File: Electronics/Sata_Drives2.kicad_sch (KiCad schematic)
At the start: 66 parts, among them J20 0877131001, J21 0877131001, Q10 NPN, Q11 PMOS, Q12 NPN, Q13 PMOS, Q14 PMOS, Q15 NPN, Q16 PMOS, Q17 NPN, U11 W25X40CLSN, U12 JMS561, Y2 30MHz

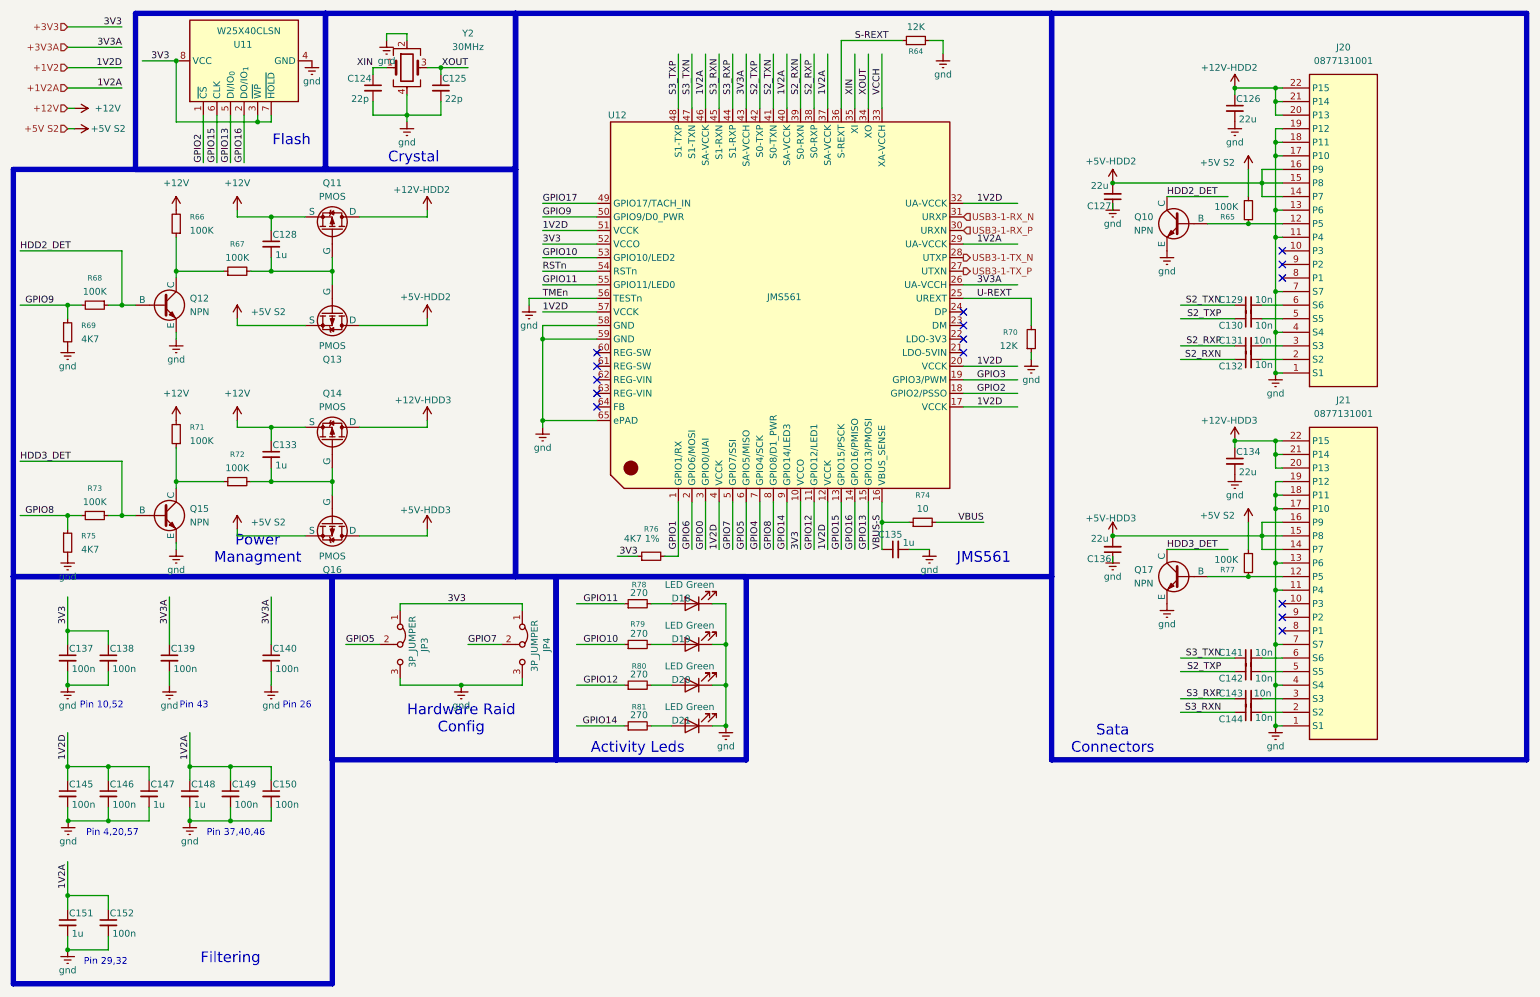
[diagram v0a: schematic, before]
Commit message: More pcb arangment, verticle ports
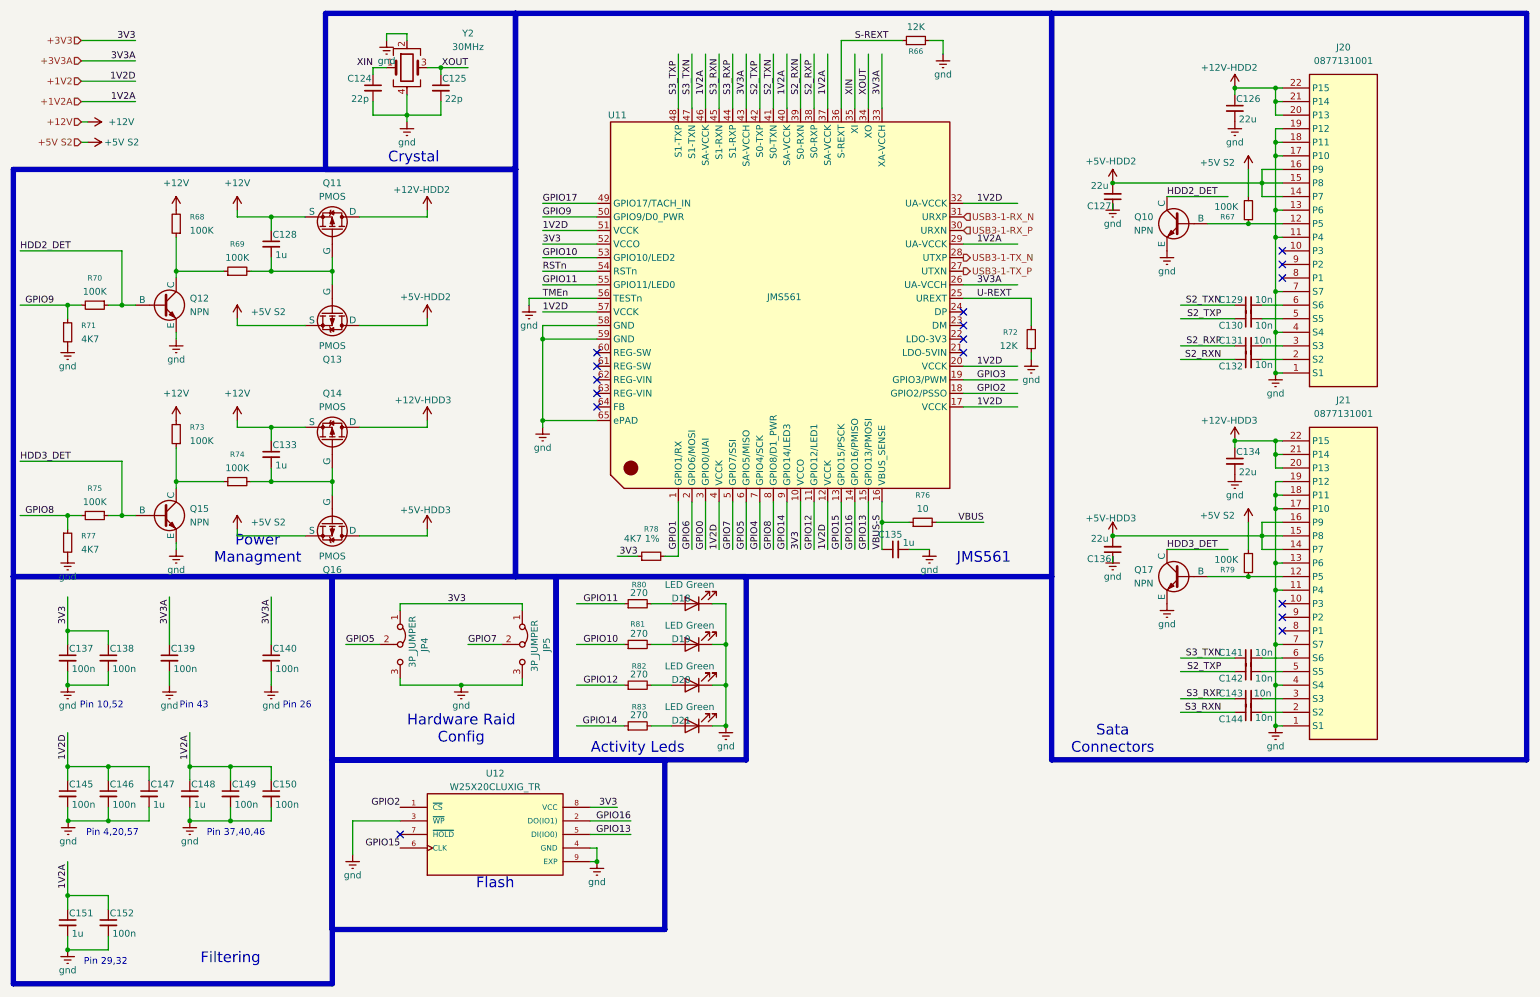
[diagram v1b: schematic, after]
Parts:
- removed U11: W25X40CLSN, Package_SO:SOIC-8_3.9x4.9mm_P1.27mm, symbol Memory_Flash:W25X40CLSN
- added U12: W25X20CLUXIG_TR, W25X20CLUXIG_TR:SON50P300X200X60-9N, symbol W25X20CLUXIG_TR:W25X20CLUXIG_TR
- renumbered JP3 to JP4, JP4 to JP5, R64 to R66, R65 to R67, R66 to R68, R67 to R69, R68 to R70, R69 to R71, R70 to R72, R71 to R73, R72 to R74, R73 to R75, R74 to R76, R75 to R77, R76 to R78, R77 to R79, R78 to R80, R79 to R81, R80 to R82, R81 to R83, U12 to U11
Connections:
- net VCCH is gone; now on net +3V3A: U11.33 (XA-VCCH)
- net +3V3: now also U12.8 (VCC)
- net GPIO13: now also U12.5 (DI(IO0))
- net GPIO15: now also U12.6 (CLK)
- net GPIO16: now also U12.2 (DO(IO1))
- net GPIO2: now also U12.1 (~{CS})
- net gnd: now also U12.3 (~{WP}), U12.4 (GND), U12.9 (EXP)
- no-connect marks 15 -> 16

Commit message: Power symbols changed and sata hub fixed schem
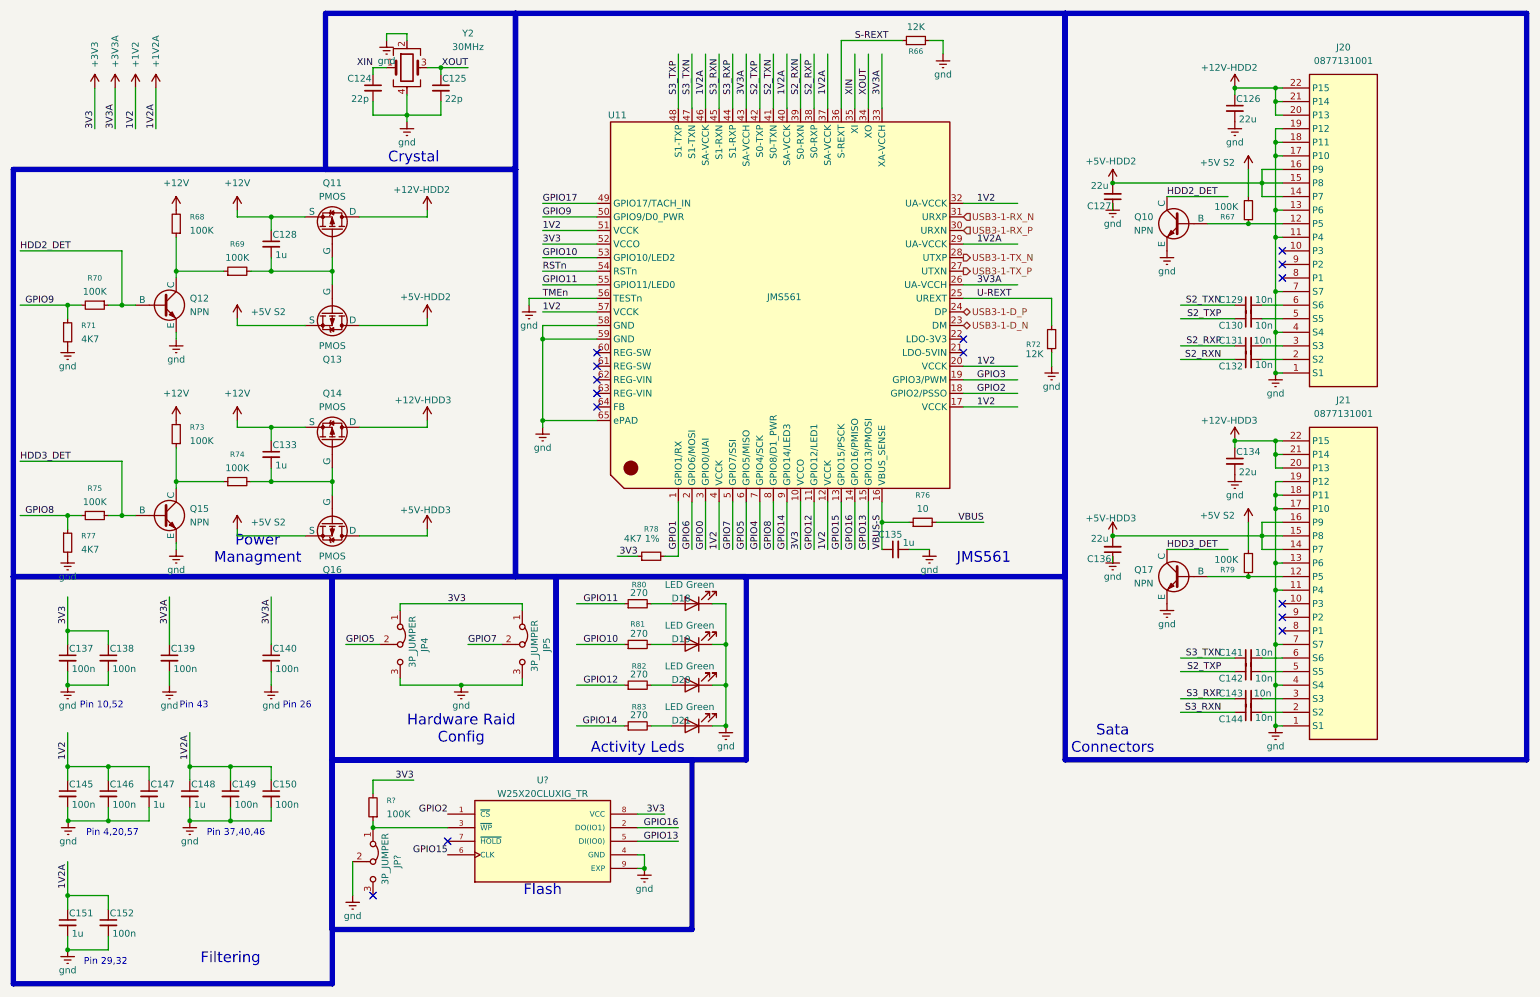
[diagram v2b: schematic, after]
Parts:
- removed U12: W25X20CLUXIG_TR, W25X20CLUXIG_TR:SON50P300X200X60-9N, symbol W25X20CLUXIG_TR:W25X20CLUXIG_TR
- added JP?: 3P_JUMPER, Connector_PinHeader_2.54mm:PinHeader_1x03_P2.54mm_Vertical, symbol Jumper:Jumper_3_Bridged12
- added R?: 100K, Resistor_SMD:R_0603_1608Metric, symbol Device:R_Small
- added U?: W25X20CLUXIG_TR, W25X20CLUXIG_TR:SON50P300X200X60-9N, symbol W25X20CLUXIG_TR:W25X20CLUXIG_TR
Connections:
- net +3V3: now also R?.2, U?.8 (VCC)
- net GPIO13: now also U?.5 (DI(IO0))
- net GPIO15: now also U?.6 (CLK)
- net GPIO16: now also U?.2 (DO(IO1))
- net GPIO2: now also U?.1 (~{CS})
- net gnd: now also JP?.2 (C), U?.4 (GND), U?.9 (EXP)
- net USB3-1-D_N: now reaches U11.23 (DM)
- net USB3-1-D_P: now reaches U11.24 (DP)
- new net: JP?.1 (A), R?.1, U?.3 (~{WP})
- no-connect marks 16 -> 15
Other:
- moved on the sheet: R72

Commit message: Fans
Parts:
- gave numbers to parts that had none: 3
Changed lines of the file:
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@@
 		(dnp no)
 		(fields_autoplaced yes)
-		(property "Reference" "U?"
+		(property "Reference" "U12"
 			(at 111.76 157.48 0)
 			(effects
@@
 			(project "CM5 Nas"
 				(path "/0650c7a8-acba-429c-9f8e-eec0baf0bc1c/fede4c36-00cc-4d3d-b71c-5243ba232202/39c281b2-2608-4942-ba08-2308e06d446a"
-					(reference "U?")
+					(reference "U12")
 					(unit 1)
 				)
@@
 		(on_board yes)
 		(dnp no)
-		(property "Reference" "JP?"
+		(property "Reference" "JP6"
 			(at 84.582 171.45 0)
 			(effects
@@
 			(project "CM5 Nas"
 				(path "/0650c7a8-acba-429c-9f8e-eec0baf0bc1c/fede4c36-00cc-4d3d-b71c-5243ba232202/39c281b2-2608-4942-ba08-2308e06d446a"
-					(reference "JP?")
+					(reference "JP6")
 					(unit 1)
 				)
@@
 		(dnp no)
 		(fields_autoplaced yes)
-		(property "Reference" "R?"
+		(property "Reference" "R85"
 			(at 82.55 161.2899 0)
 			(effects
@@
 			(project "CM5 Nas"
 				(path "/0650c7a8-acba-429c-9f8e-eec0baf0bc1c/fede4c36-00cc-4d3d-b71c-5243ba232202/39c281b2-2608-4942-ba08-2308e06d446a"
-					(reference "R?")
+					(reference "R85")
 					(unit 1)
 				)
